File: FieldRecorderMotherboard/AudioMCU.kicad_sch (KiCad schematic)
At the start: 2 parts, among them U1 STM32H723ZGTx, U2 PCM1860DBT

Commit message: note
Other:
- note added: "The memory is APS12808L"

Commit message: firmware bones
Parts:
- added U3: APS12808L, Package_BGA:miniBGA-24_6x8mm_Layout5x5_P1.0mm, symbol Memory_RAM:APS12808L-3OBMx

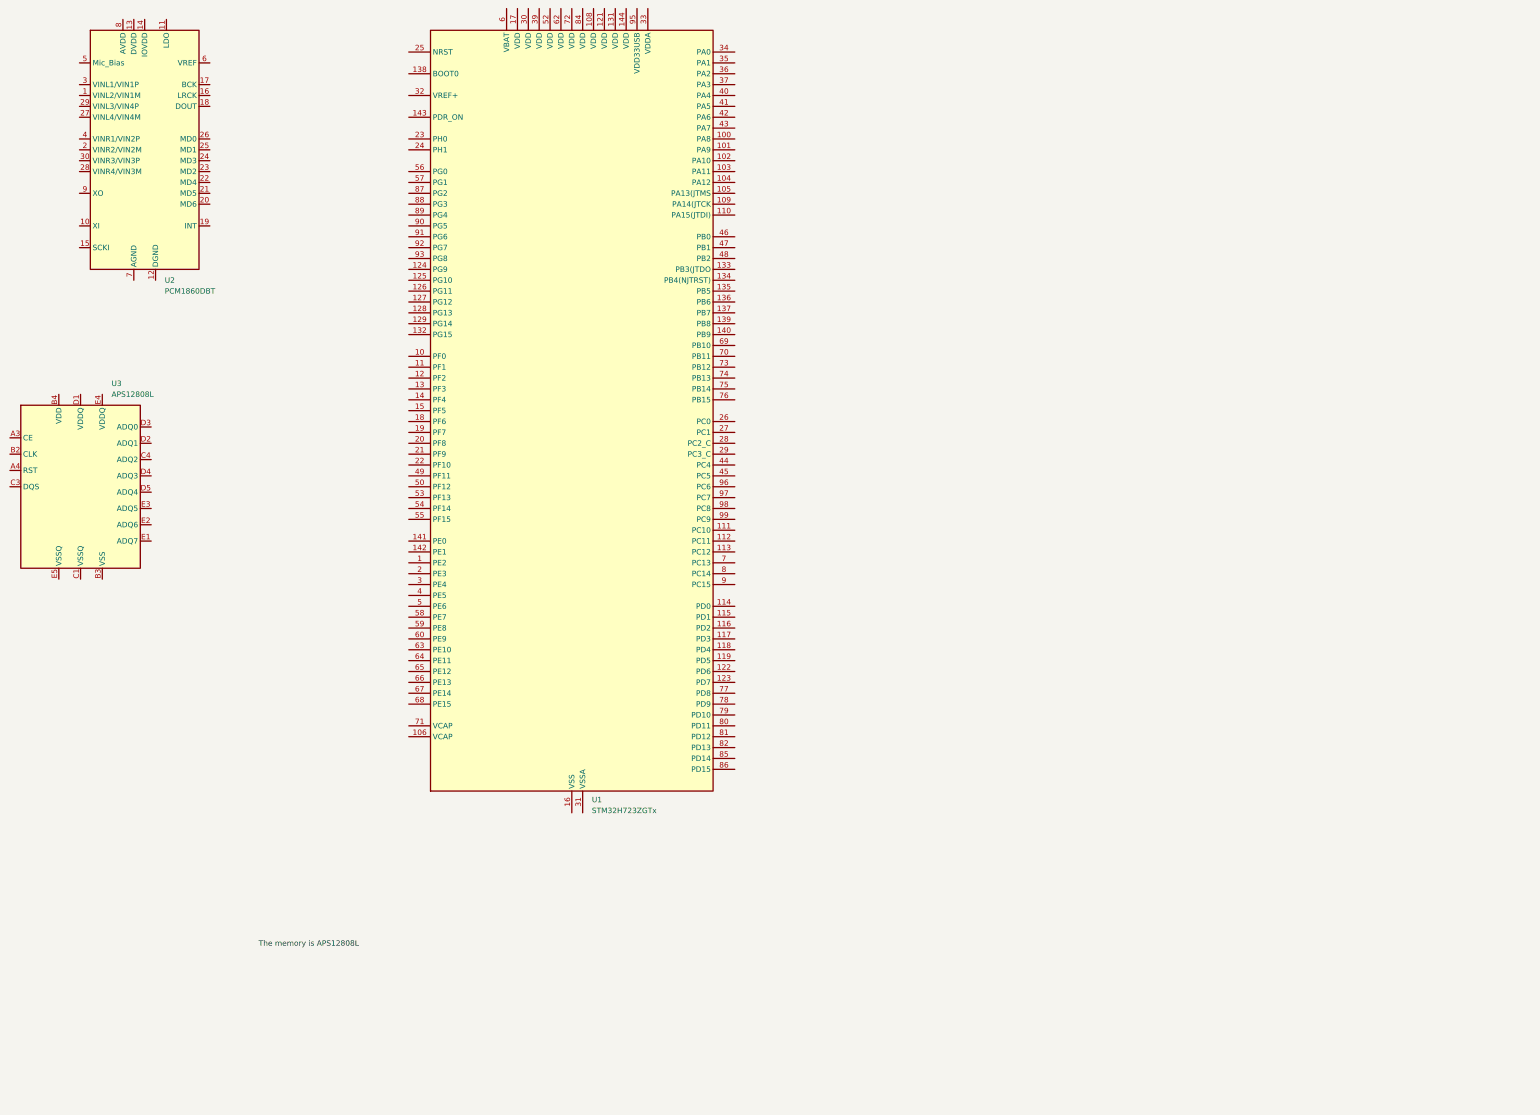
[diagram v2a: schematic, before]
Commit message: pinout changes, USB chip
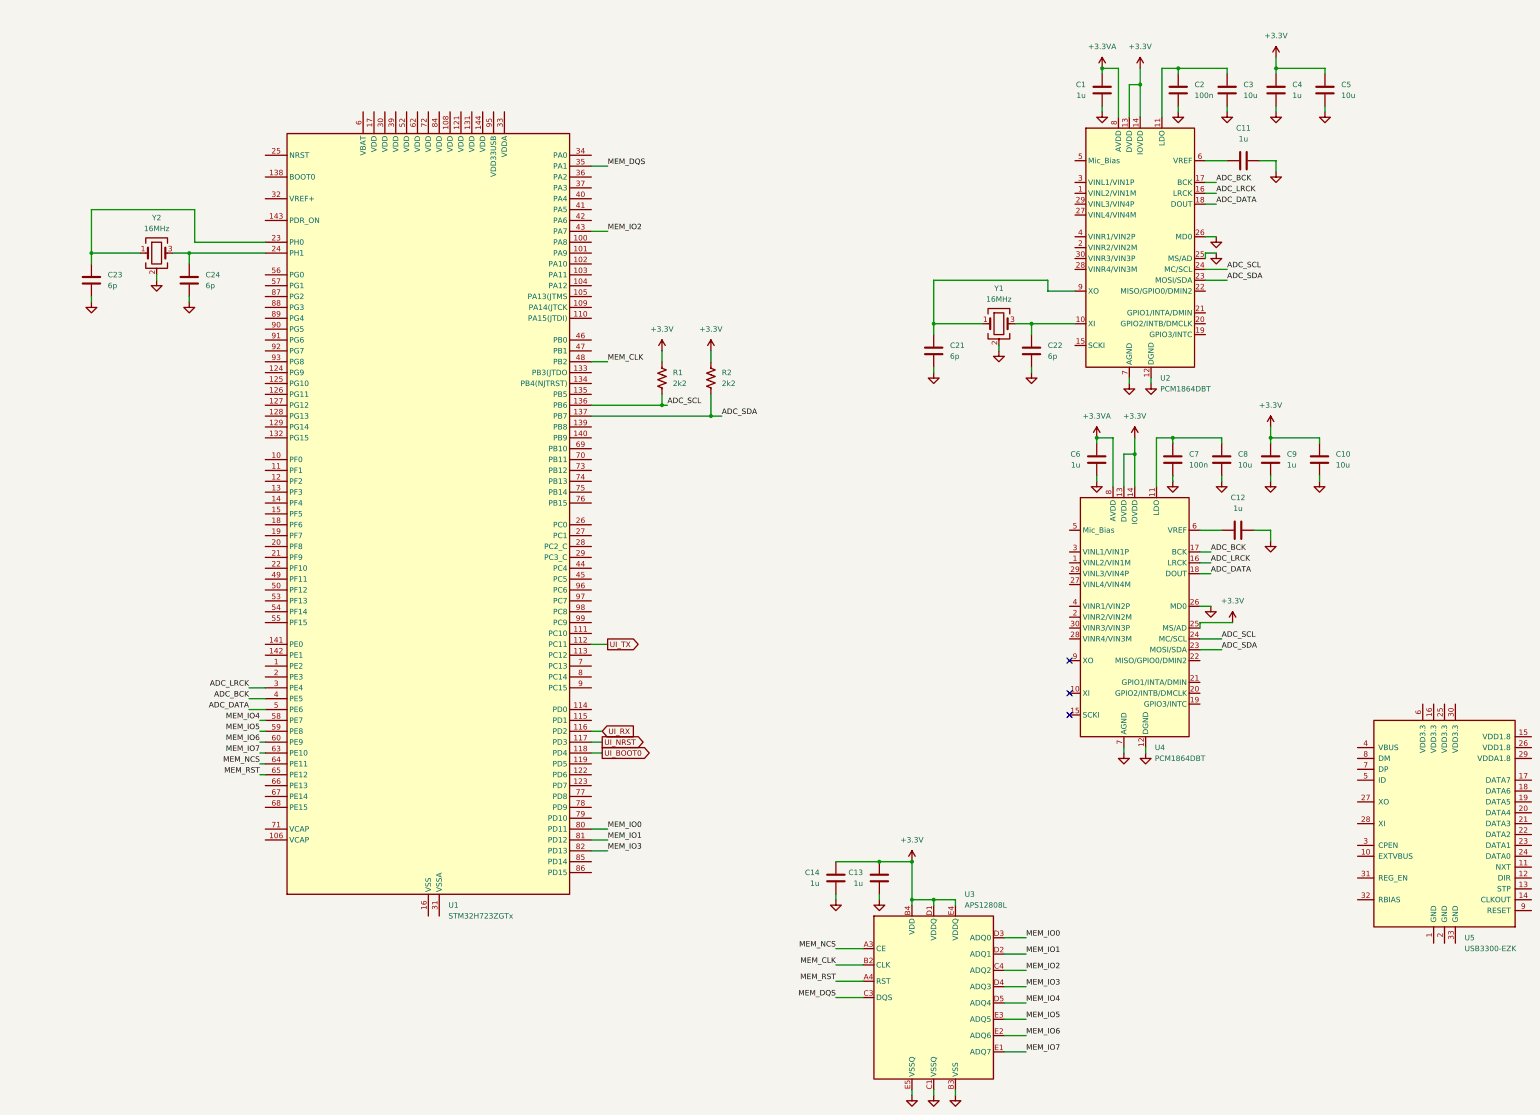
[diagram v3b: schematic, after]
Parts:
- removed U2: PCM1860DBT, Package_SO:TSSOP-30_4.4x7.8mm_P0.5mm, symbol Audio:PCM1860DBT
- added C1, C11, C12, C13, C14, C4, C6, C9: 1u, symbol Device:C
- added C10, C3, C5, C8: 10u, symbol Device:C
- added C2, C7: 100n, symbol Device:C
- added C21, C22, C23, C24: 6p, Capacitor_SMD:C_0805_2012Metric, symbol Device:C
- added R1, R2: 2k2, symbol Device:R_US
- added U2, U4: PCM1864DBT, Package_SO:TSSOP-30_4.4x7.8mm_P0.5mm, symbol Audio:PCM1864DBT
- added U5: USB3300-EZK, Package_DFN_QFN:QFN-32-1EP_5x5mm_P0.5mm_EP3.45x3.45mm, symbol Interface_USB:USB3300-EZK
- added Y1, Y2: 16MHz, Crystal:Crystal_SMD_3225-4Pin_3.2x2.5mm, symbol Device:Crystal_GND24
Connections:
- net MEM_NCS: now reaches U3.A3 (CE)
- net MEM_NCS: now also U1.64 (PE11)
- net MEM_RST: now reaches U3.A4 (RST)
- net MEM_RST: now also U1.65 (PE12)
- net MEM_CLK: now reaches U3.B2 (CLK)
- net MEM_CLK: now also U1.48 (PB2)
- net GND: now reaches U3.B3 (VSS)
- net GND: now also U3.C1 (VSSQ), U3.E5 (VSSQ), C1.2, C10.2, C11.2, C12.2, C13.2, C14.2, C2.2, C21.1, C22.1, C23.1, C24.1, C3.2, C4.2, C5.2, C6.2, C7.2, C8.2, C9.2, U2.12 (DGND), U2.25 (MS/AD), U2.26 (MD0), U2.7 (AGND), U4.12 (DGND), U4.26 (MD0), U4.7 (AGND), Y1.2 (G), Y1.4 (G), Y2.2 (G), Y2.4 (G)
- net +3.3V: now reaches U3.B4 (VDD)
- net +3.3V: now also U3.D1 (VDDQ), U3.E4 (VDDQ), C10.1, C13.1, C14.1, C4.1, C5.1, C9.1, R1.1, R2.1, U2.13 (DVDD), U2.14 (IOVDD), U4.13 (DVDD), U4.14 (IOVDD), U4.25 (MS/AD)
- net MEM_DQS: now reaches U3.C3 (DQS)
- net MEM_DQS: now also U1.35 (PA1)
- net MEM_IO2: now reaches U3.C4 (ADQ2)
- net MEM_IO2: now also U1.43 (PA7)
- net MEM_IO1: now reaches U3.D2 (ADQ1)
- net MEM_IO1: now also U1.81 (PD12)
- net MEM_IO0: now reaches U3.D3 (ADQ0)
- net MEM_IO0: now also U1.80 (PD11)
- net MEM_IO3: now reaches U3.D4 (ADQ3)
- net MEM_IO3: now also U1.82 (PD13)
- net MEM_IO4: now reaches U3.D5 (ADQ4)
- net MEM_IO4: now also U1.58 (PE7)
- net MEM_IO7: now reaches U3.E1 (ADQ7)
- net MEM_IO7: now also U1.63 (PE10)
- net MEM_IO6: now reaches U3.E2 (ADQ6)
- net MEM_IO6: now also U1.60 (PE9)
- net MEM_IO5: now reaches U3.E3 (ADQ5)
- net MEM_IO5: now also U1.59 (PE8)
- net UI_TX: now reaches U1.112 (PC11)
- net UI_RX: now reaches U1.116 (PD2)
- net UI_NRST: now reaches U1.117 (PD3)
- net UI_BOOT0: now reaches U1.118 (PD4)
- net ADC_SCL: now reaches U1.136 (PB6)
- net ADC_SCL: now also R1.2, U2.24 (MC/SCL), U4.24 (MC/SCL)
- net ADC_SDA: now reaches U1.137 (PB7)
- net ADC_SDA: now also R2.2, U2.23 (MOSI/SDA), U4.23 (MOSI/SDA)
- net at U1.23 (PH0): now also C23.2, Y2.1
- net at U1.24 (PH1): now also C24.2, Y2.3
- net ADC_LRCK: now reaches U1.3 (PE4)
- net ADC_LRCK: now also U2.16 (LRCK), U4.16 (LRCK)
- net ADC_BCK: now reaches U1.4 (PE5)
- net ADC_BCK: now also U2.17 (BCK), U4.17 (BCK)
- net ADC_DATA: now reaches U1.5 (PE6)
- net ADC_DATA: now also U2.18 (DOUT), U4.18 (DOUT)
- new net: C7.1, C8.1, U4.11 (LDO)
- new net: C12.1, U4.6 (VREF)
- new net: C11.1, U2.6 (VREF)
- new net: C21.2, U2.9 (XO), Y1.1
- new net: C22.2, U2.10 (XI), Y1.3
- new net: C2.1, C3.1, U2.11 (LDO)
- new net +3.3VA: C1.1, C6.1, U2.8 (AVDD), U4.8 (AVDD)
- no-connect marks 0 -> 3
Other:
- note removed: "The memory is APS12808L"
- moved on the sheet: U1, U3

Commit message: morning expansions
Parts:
- added C15, C16: 2u2, symbol Device:C
- added C25, C26, C27, C28, C31, C32: 1u, Capacitor_SMD:C_0805_2012Metric, symbol Device:C
- added C29, C30: 6p, Capacitor_SMD:C_0805_2012Metric, symbol Device:C
- added C33: 4n7, Capacitor_SMD:C_0805_2012Metric, symbol Device:C
- added D1: SMAJ5.0A, Diode_SMD:D_SMA, symbol Diode:SMAJ5.0A
- added J1: USB_C_Receptacle_USB2.0_16P, Connector_USB:USB_C_Receptacle_G-Switch_GT-USB-7010ASV, symbol Connector:USB_C_Receptacle_USB2.0_16P_Ergo
- added J2: SD_Card_Receptacle, Connector_Card:SD_Kyocera_145638009211859+, symbol Connector:SD_Card_Receptacle
- added Q1: MMFTP3401, Package_TO_SOT_SMD:SOT-23, symbol Transistor_FET:AO3401A
- added Q2, Q3: 2N7002, Package_TO_SOT_SMD:SOT-23, symbol Transistor_FET:2N7002
- added R10: 100k, symbol Device:R_US
- added R11: 100, symbol Device:R_US
- added R12, R13: 22k, symbol Device:R_US
- added R3: 12.0k 1%, symbol Device:R_US
- added R4: 820, symbol Device:R_US
- added R5, R6: 5k1, symbol Device:R_US
- added R7: 1Meg, symbol Device:R_US
- added R8: 0R, symbol Device:R_US
- added RN1: 22k, symbol Device:R_Pack04
- added U6: USBLC6-2SC6, Package_TO_SOT_SMD:SOT-23-6, symbol Power_Protection:USBLC6-2SC6
- added Y3: 24Mhz, Crystal:Crystal_SMD_3225-4Pin_3.2x2.5mm, symbol Device:Crystal_GND24
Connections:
- net +3.3V: now also U5.16 (VDD3.3), U5.25 (VDD3.3), U5.30 (VDD3.3), U5.31 (REG_EN), U5.6 (VDD3.3), C25.2, C26.2, Q1.3 (D), R10.1, R13.1
- net GND: now also U1.107 (VSS), U1.120 (VSS), U1.130 (VSS), U1.16 (VSS), U1.31 (VSSA), U1.38 (VSS), U1.51 (VSS), U1.61 (VSS), U1.83 (VSS), U1.94 (VSS), U5.1 (GND), U5.2 (GND), U5.33 (GND), U5.9 (RESET), C15.2, C16.2, C25.1, C26.1, C27.1, C28.1, C29.1, C30.1, C31.1, C32.1, C33.1, D1.2 (A2), J1.A1 (GND), J1.A12 (GND), J1.B1 (GND), J1.B12 (GND), J2.3 (VSS), J2.6 (VSS), Q2.2 (S), Q3.2 (S), R3.2, R5.2, R6.2, R7.2, R8.2, U6.2 (GND), Y3.2 (G), Y3.4 (G)
- net UI_TX: now also U1.113 (PC12); no longer U1.112 (PC11)
- net SWDIO: now reaches U1.105 (PA13(JTMS)
- net at U1.106 (VCAP): now also C15.1
- net SWCLK: now reaches U1.109 (PA14(JTCK)
- net SD_CK: now reaches U1.122 (PD6)
- net SD_CK: now also J2.5 (CLK)
- net SD_CMD: now reaches U1.123 (PD7)
- net SD_CMD: now also J2.2 (CMD), R12.2
- net SD_D0: now reaches U1.124 (PG9)
- net SD_D0: now also J2.7 (DAT0), RN1.1 (R1.1)
- net SD_D1: now reaches U1.125 (PG10)
- net SD_D1: now also J2.8 (DAT1), RN1.2 (R2.1)
- net SD_D2: now reaches U1.126 (PG11)
- net SD_D2: now also J2.9 (DAT2), RN1.3 (R3.1)
- net SD_D3: now reaches U1.127 (PG12)
- net SD_D3: now also J2.1 (CD/DAT3), RN1.4 (R4.1)
- net SD_DETECT: now reaches U1.128 (PG13)
- net SD_DETECT: now also J2.10 (CARD_DETECT), R13.2
- net SD_PWR: now reaches U1.129 (PG14)
- net SD_PWR: now also Q2.1 (G)
- net USB_D7: now reaches U1.135 (PB5)
- net USB_D7: now also U5.17 (DATA7)
- net USB_STP: now reaches U1.26 (PC0)
- net USB_STP: now also U5.13 (STP)
- net USB_DIR: now reaches U1.28 (PC2_C)
- net USB_DIR: now also U5.12 (DIR)
- net USB_NXT: now reaches U1.29 (PC3_C)
- net USB_NXT: now also U5.11 (NXT)
- net USB_D0: now reaches U1.37 (PA3)
- net USB_D0: now also U5.24 (DATA0)
- net USB_CK: now reaches U1.41 (PA5)
- net USB_CK: now also U5.14 (CLKOUT)
- net USB_D1: now reaches U1.46 (PB0)
- net USB_D1: now also U5.23 (DATA1)
- net USB_D2: now reaches U1.47 (PB1)
- net USB_D2: now also U5.22 (DATA2)
- net USB_D3: now reaches U1.69 (PB10)
- net USB_D3: now also U5.21 (DATA3)
- net USB_D4: now reaches U1.70 (PB11)
- net USB_D4: now also U5.20 (DATA4)
- net at U1.71 (VCAP): now also C16.1
- net USB_D5: now reaches U1.73 (PB12)
- net USB_D5: now also U5.19 (DATA5)
- net USB_D6: now reaches U1.74 (PB13)
- net USB_D6: now also U5.18 (DATA6)
- net at U5.15 (VDD1.8): now also U5.26 (VDD1.8), C31.2
- net at U5.27 (XO): now also C29.2, Y3.1
- net at U5.28 (XI): now also C30.2, Y3.3
- net at U5.29 (VDDA1.8): now also C32.2
- net at U5.32 (RBIAS): now also R3.1
- net at U5.4 (VBUS): now also R4.2
- net USB_D+: now reaches U5.7 (DP)
- net USB_D+: now also U6.4 (I/O2)
- net USB_D-: now reaches U5.8 (DM)
- net USB_D-: now also U6.6 (I/O1)
- new net: C33.2, J1.SH (SHIELD), R7.1, R8.1
- new net: J1.A5 (CC1), R6.1
- new net: J1.A6 (D+), J1.B6 (D+), U6.3 (I/O2)
- new net: J1.A7 (D-), J1.B7 (D-), U6.1 (I/O1)
- new net: J1.B5 (CC2), R5.1
- new net: Q1.1 (G), Q2.3 (D), Q3.1 (G), R10.2
- new net: Q3.3 (D), R11.2
- new net USB_VBUS: C27.2, D1.1 (A1), J1.A4 (VBUS), J1.A9 (VBUS), J1.B4 (VBUS), J1.B9 (VBUS), R4.1, U6.5 (VBUS)
- new net VCC_SD: C28.2, J2.4 (VDD), Q1.2 (S), R11.1, R12.1, RN1.5 (R4.2), RN1.6 (R3.2), RN1.7 (R2.2), RN1.8 (R1.2)
- no-connect marks 3 -> 10
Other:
- note added: "TODO: find actual values for C29 and C30"
- moved on the sheet: C1, C10, C11, C12, C2, C21, C22, C23, C24, C3, C4, C5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
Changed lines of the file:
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@@
 	(generator "eeschema")
 	(generator_version "10.0")
-	(paper "A3")
+	(paper "A2")

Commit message: odds, ends, etc
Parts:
- removed J1: USB_C_Receptacle_USB2.0_16P, Connector_USB:USB_C_Receptacle_G-Switch_GT-USB-7010ASV, symbol Connector:USB_C_Receptacle_USB2.0_16P_Ergo
- removed U6: USBLC6-2SC6, Package_TO_SOT_SMD:SOT-23-6, symbol Power_Protection:USBLC6-2SC6
- added C17, C19, C34, C35, C36, C37, C38, C39, C40, C41, C42, C43, C44, C45, C46, C48: 1u, Capacitor_SMD:C_0805_2012Metric, symbol Device:C
- added C18, C20, C47, C49: 10u, Capacitor_SMD:C_0805_2012Metric, symbol Device:C
- added C50: 2u2, Capacitor_SMD:C_0805_2012Metric, symbol Device:C
- added J1: USB_C_Receptacle_USB2.0_16P, symbol Connector:USB_C_Receptacle_USB2.0_16P
- added R14: 22k, Resistor_SMD:R_0805_2012Metric, symbol Device:R_US
- added R9: 47, Resistor_SMD:R_0805_2012Metric, symbol Device:R_US
- added U6: USBLC6-4SC6, Package_TO_SOT_SMD:SOT-23-6, symbol Power_Protection:USBLC6-4SC6
- added U7: PCM5100A, Package_SO:TSSOP-20_4.4x6.5mm_P0.65mm, symbol Audio:PCM5100A
- C1, C10, C11, C12, C13, C14, C15, C16, C2, C3, C4, C5, C6, C7, C8, C9: footprint (none) -> Capacitor_SMD:C_0805_2012Metric
- R1, R10, R11, R12, R13, R2, R3, R4, R5, R6, R7, R8: footprint (none) -> Resistor_SMD:R_0805_2012Metric
- RN1: footprint (none) -> Resistor_SMD:R_Array_Concave_4x0603
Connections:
- net +3.3V: now also U1.108 (VDD), U1.121 (VDD), U1.131 (VDD), U1.144 (VDD), U1.17 (VDD), U1.30 (VDD), U1.39 (VDD), U1.52 (VDD), U1.6 (VBAT), U1.62 (VDD), U1.72 (VDD), U1.84 (VDD), U1.95 (VDD33USB), C19.1, C20.1, C34.2, C35.2, C36.2, C37.2, C38.2, C39.2, C40.2, C41.2, C42.2, C43.2, C44.2, C45.2, R14.1, R9.1, U7.20 (DVDD)
- net +3.3VA: now also U1.33 (VDDA), C17.1, C18.1, C46.2, C47.2, R9.2, U7.1 (CPVDD), U7.8 (AVDD)
- net GND: now also C17.2, C18.2, C19.2, C20.2, C34.1, C35.1, C36.1, C37.1, C38.1, C39.1, C40.1, C41.1, C42.1, C43.1, C44.1, C45.1, C46.1, C47.1, C48.2, C49.2, J1.A1 (GND), J1.A12 (GND), J1.B1 (GND), J1.B12 (GND), U6.2 (GND), U7.10 (DEMP), U7.11 (FLT), U7.12 (SCK), U7.16 (FMT), U7.19 (DGND), U7.3 (CPGND), U7.9 (AGND)
- net USB_D+: now also J1.A6 (D+), J1.B6 (D+), U6.6 (I/O4)
- net USB_D-: now also J1.A7 (D-), J1.B7 (D-), U6.4 (I/O3)
- net USB_VBUS: now also J1.A4 (VBUS), J1.A9 (VBUS), J1.B4 (VBUS), J1.B9 (VBUS), U6.5 (VBUS)
- net at C33.2, R7.1, R8.1: now also J1.SH (SHIELD)
- net CC1: now reaches R6.1
- net CC1: now also J1.A5 (CC1), U6.1 (I/O1)
- net CC2: now reaches R5.1
- net CC2: now also J1.B5 (CC2), U6.3 (I/O2)
- net DAC_NMUTE: now reaches U1.100 (PA8)
- net DAC_NMUTE: now also R14.2, U7.17 (XSMT)
- net DAC_BCK: now reaches U1.101 (PA9)
- net DAC_BCK: now also U7.13 (BCK)
- net DAC_LR: now reaches U1.103 (PA11)
- net DAC_LR: now also U7.15 (LRCK)
- net NRST: now reaches U1.25 (NRST)
- net DAC_SDO: now reaches U1.76 (PB15)
- net DAC_SDO: now also U7.14 (DIN)
- new net: C50.1, U7.2 (CAPP)
- new net: C50.2, U7.4 (CAPM)
- new net: C48.1, C49.1, U7.18 (LDOO)
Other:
- moved on the sheet: C13, C14, C15, C16, C23, C24, C25, C26, C27, C28, C29, C30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
